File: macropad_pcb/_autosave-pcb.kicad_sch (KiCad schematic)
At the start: 123 parts, among them U1 Raspberry_Pi_Pico

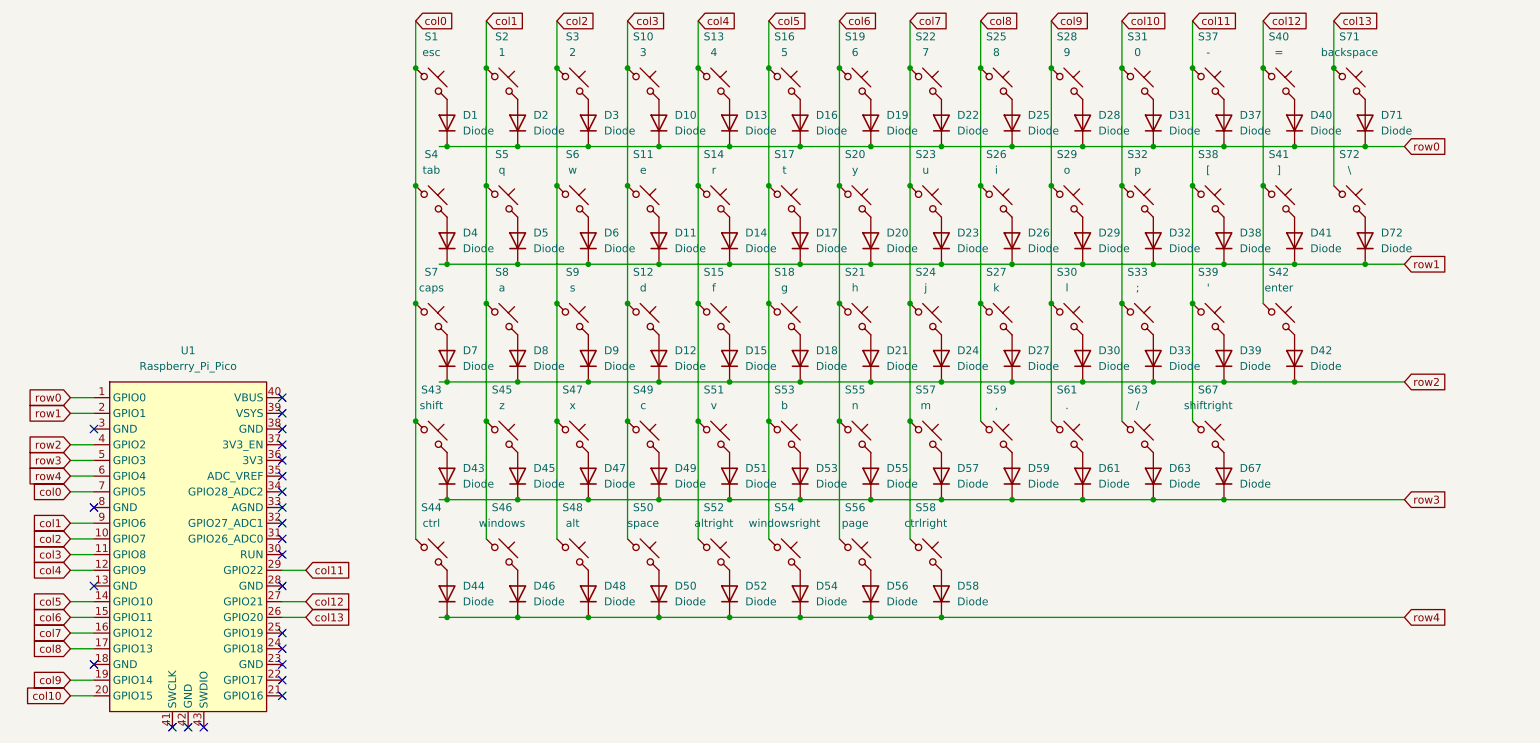
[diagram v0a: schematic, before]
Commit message: still making the full 72 sized keyboard pcb
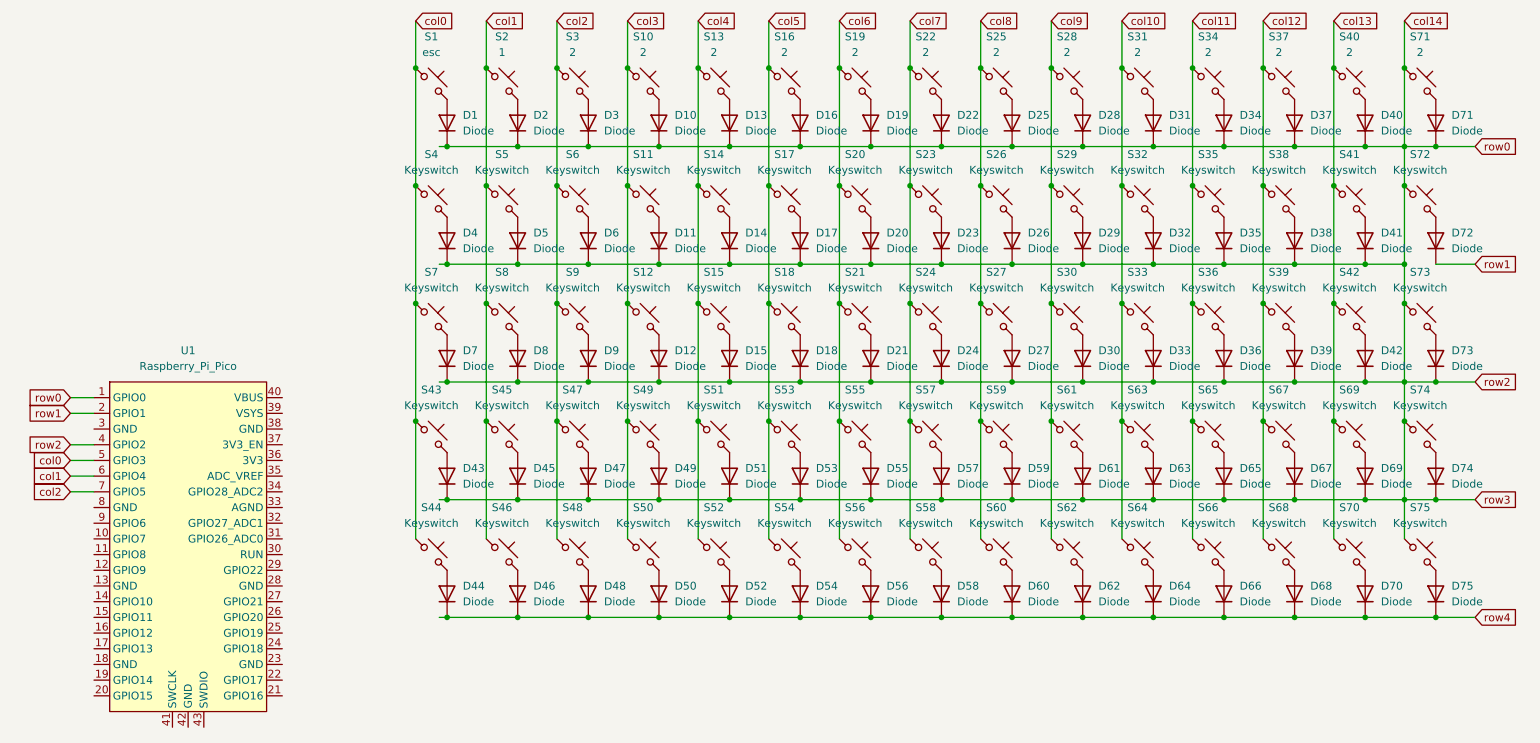
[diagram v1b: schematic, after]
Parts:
- added D34, D35, D36, D60, D62, D64, D65, D66, D68, D69, D70, D73, D74, D75: Diode, ScottoKeebs_Components:Diode_DO-35, symbol ScottoKeebs:Placeholder_Diode
- added S34: 2, ScottoKeebs_MX:MX_PCB_1.00u, symbol ScottoKeebs:Placeholder_Keyswitch
- added S35, S36, S60, S62, S64, S65, S66, S68, S69, S70, S73, S74, S75: Keyswitch, ScottoKeebs_MX:MX_PCB_1.00u, symbol ScottoKeebs:Placeholder_Keyswitch
- S10: value 3 -> 2
- S11: value e -> Keyswitch
- S12: value d -> Keyswitch
- S13: value 4 -> 2
- S14: value r -> Keyswitch
- S15: value f -> Keyswitch
- S16: value 5 -> 2
- S17: value t -> Keyswitch
- S18: value g -> Keyswitch
- S19: value 6 -> 2
- S20: value y -> Keyswitch
- S21: value h -> Keyswitch
- S22: value 7 -> 2
- S23: value u -> Keyswitch
- S24: value j -> Keyswitch
- S25: value 8 -> 2
- S26: value i -> Keyswitch
- S27: value k -> Keyswitch
- S28: value 9 -> 2
- S29: value o -> Keyswitch
- S30: value l -> Keyswitch
- S31: value 0 -> 2
- S32: value p -> Keyswitch
- S33: value ; -> Keyswitch
- S37: value - -> 2
- S38: value [ -> Keyswitch
- S39: value ' -> Keyswitch
- S4: value tab -> Keyswitch
- S40: value = -> 2
- S41: value ] -> Keyswitch
- S42: value enter -> Keyswitch
- S43: value shift -> Keyswitch
- S44: value ctrl -> Keyswitch
- S45: value z -> Keyswitch
- S46: value windows -> Keyswitch
- S47: value x -> Keyswitch
- S48: value alt -> Keyswitch
- S49: value c -> Keyswitch
- S5: value q -> Keyswitch
- S50: value space -> Keyswitch
- S51: value v -> Keyswitch
- S52: value altright -> Keyswitch
- S53: value b -> Keyswitch
- S54: value windowsright -> Keyswitch
- S55: value n -> Keyswitch
- S56: value page -> Keyswitch
- S57: value m -> Keyswitch
- S58: value ctrlright -> Keyswitch
- S59: value , -> Keyswitch
- S6: value w -> Keyswitch
- S61: value . -> Keyswitch
- S63: value / -> Keyswitch
- S67: value shiftright -> Keyswitch
- S7: value caps -> Keyswitch
- S71: value backspace -> 2
- S72: value \ -> Keyswitch
- S8: value a -> Keyswitch
- S9: value s -> Keyswitch
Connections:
- net row2 is gone; now on net col14: D12.1 (K), D15.1 (K), D18.1 (K), D21.1 (K), D24.1 (K), D27.1 (K), D30.1 (K), D33.1 (K), D39.1 (K), D42.1 (K), D7.1 (K), D8.1 (K), D9.1 (K), U1.4 (GPIO2)
- net col0: now also U1.5 (GPIO3); no longer U1.7 (GPIO5)
- net col1: now also U1.6 (GPIO4); no longer U1.9 (GPIO6)
- net col10: now also S64.1; no longer U1.20 (GPIO15)
- net col11: now also S34.1, S35.1, S36.1, S65.1, S66.1; no longer S37.1, S38.1, S39.1, S67.1, U1.29 (GPIO22)
- net col12: now also S37.1, S38.1, S39.1, S67.1, S68.1; no longer S40.1, S41.1, S42.1, U1.27 (GPIO21)
- net col13: now also S40.1, S41.1, S42.1, S69.1, S70.1; no longer S71.1, S72.1, U1.26 (GPIO20)
- net col2: now also U1.7 (GPIO5); no longer U1.10 (GPIO7)
- net col3: no longer U1.11 (GPIO8)
- net col4: no longer U1.12 (GPIO9)
- net col5: no longer U1.14 (GPIO10)
- net col6: no longer U1.15 (GPIO11)
- net col7: no longer U1.16 (GPIO12)
- net col8: now also S60.1; no longer U1.17 (GPIO13)
- net col9: now also S62.1; no longer U1.19 (GPIO14)
- net row1: no longer D11.1 (K), D14.1 (K), D17.1 (K), D20.1 (K), D23.1 (K), D26.1 (K), D29.1 (K), D32.1 (K), D38.1 (K), D4.1 (K), D41.1 (K), D5.1 (K), D6.1 (K)
- net row4: now also D60.1 (K), D62.1 (K), D64.1 (K), D66.1 (K), D68.1 (K), D70.1 (K), D75.1 (K); no longer U1.6 (GPIO4)
- net row0 renamed col14
- net col14: now also D11.1 (K), D14.1 (K), D17.1 (K), D20.1 (K), D23.1 (K), D26.1 (K), D29.1 (K), D32.1 (K), D38.1 (K), D4.1 (K), D41.1 (K), D43.1 (K), D45.1 (K), D47.1 (K), D49.1 (K), D5.1 (K), D51.1 (K), D53.1 (K), D55.1 (K), D57.1 (K), D59.1 (K), D6.1 (K), D61.1 (K), D63.1 (K), D67.1 (K), S71.1, S72.1, D34.1 (K), D35.1 (K), D36.1 (K), D65.1 (K), D69.1 (K), D73.1 (K), D74.1 (K), S73.1, S74.1, S75.1
- removed net row3: D43.1 (K), D45.1 (K), D47.1 (K), D49.1 (K), D51.1 (K), D53.1 (K), D55.1 (K), D57.1 (K), D59.1 (K), D61.1 (K), D63.1 (K), D67.1 (K), U1.5 (GPIO3)
- new net: D65.2 (A), S65.2
- new net: D70.2 (A), S70.2
- new net: D62.2 (A), S62.2
- new net: D60.2 (A), S60.2
- new net: D75.2 (A), S75.2
- new net: D64.2 (A), S64.2
- new net: D35.2 (A), S35.2
- new net: D66.2 (A), S66.2
- new net: D69.2 (A), S69.2
- new net: D74.2 (A), S74.2
- new net: D34.2 (A), S34.2
- new net: D68.2 (A), S68.2
- new net: D73.2 (A), S73.2
- new net: D36.2 (A), S36.2
- no-connect marks 24 -> 0
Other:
- moved on the sheet: D37, D38, D39, D40, D41, D42, D67, D71, D72, S37, S38, S39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
